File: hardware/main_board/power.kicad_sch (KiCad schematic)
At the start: 30 parts, among them J1 USB_C_Receptacle_USB2.0_16P, J2 Conn_01x03, J3 Conn_01x03, SW1 SW_Push, U1 USBLC6-2SC6, U2 BQ24259RGER, U3 TPS7A0533PDBV

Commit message: Fix PCB routing errors, update LED and connector footprints
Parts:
- D1, D2: footprint LED_SMD:LED_0603_1608Metric -> LED_SMD:LED_0805_2012Metric
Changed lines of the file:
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@@
 			)
 		)
-		(property "Footprint" "LED_SMD:LED_0603_1608Metric"
+		(property "Footprint" "LED_SMD:LED_0805_2012Metric"
 			(at 152.4 54.61 0)
 			(effects
@@
 			)
 		)
-		(property "Footprint" "LED_SMD:LED_0603_1608Metric"
+		(property "Footprint" "LED_SMD:LED_0805_2012Metric"
 			(at 142.24 54.61 0)
 			(effects

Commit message: Route 4-layer PCB
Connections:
- net D+: now also U1.1 (I/O1); no longer U1.3 (I/O2)
- net D-: now also U1.3 (I/O2); no longer U1.1 (I/O1)
- net USBCONN_D+: now also U1.6 (I/O1); no longer U1.4 (I/O2)
- net USBCONN_D-: now also U1.4 (I/O2); no longer U1.6 (I/O1)
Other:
- moved on the sheet: U1
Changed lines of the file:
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@@
 	(wire
 		(pts
-			(xy 59.69 127) (xy 59.69 125.73)
+			(xy 77.47 127) (xy 77.47 125.73)
 		)
 		(stroke
@@
 	(wire
 		(pts
-			(xy 59.69 125.73) (xy 62.23 125.73)
+			(xy 77.47 125.73) (xy 74.93 125.73)
 		)
 		(stroke
@@
 	(hierarchical_label "VBUS"
 		(shape input)
-		(at 74.93 125.73 0)
+		(at 62.23 125.73 180)
 		(effects
 			(font
 				(size 1.27 1.27)
 			)
-			(justify left)
+			(justify right)
 		)
 	)
@@
 	(symbol
 		(lib_id "power:GND")
-		(at 59.69 127 0)
+		(at 77.47 127 0)
+		(mirror y)
 		(unit 1)
 		(exclude_from_sim no)
@@
 		(fields_autoplaced yes)
 		(property "Reference" "#PWR3"
-			(at 59.69 133.35 0)
+			(at 77.47 133.35 0)
 			(effects
 				(font
@@
 		)
 		(property "Value" "GND"
-			(at 59.69 132.08 0)
+			(at 77.47 132.08 0)
 			(effects
 				(font
@@
 		)
 		(property "Footprint" ""
-			(at 59.69 127 0)
+			(at 77.47 127 0)
 			(effects
 				(font
@@
 		)
 		(property "Datasheet" ""
-			(at 59.69 127 0)
+			(at 77.47 127 0)
 			(effects
 				(font
@@
 		)
 		(property "Description" "Power symbol creates a global label with name \"GND\" , ground"
-			(at 59.69 127 0)
+			(at 77.47 127 0)
 			(effects
 				(font
@@
 	(symbol
 		(lib_id "Power_Protection:USBLC6-2SC6")
-		(at 69.85 125.73 270)
-		(mirror x)
+		(at 67.31 125.73 90)
 		(unit 1)
 		(exclude_from_sim no)
@@
 		(dnp no)
 		(property "Reference" "U1"
-			(at 79.756 122.428 90)
+			(at 58.674 129.794 90)
 			(effects
 				(font
@@
 		)
 		(property "Value" "USBLC6-2SC6"
-			(at 79.756 119.888 90)
+			(at 58.42 131.826 90)
 			(effects
 				(font
@@
 		)
 		(property "Footprint" "Package_TO_SOT_SMD:SOT-23-6"
-			(at 63.5 124.46 0)
+			(at 73.66 124.46 0)
 			(effects
 				(font
@@
 		)
 		(property "Datasheet" "https://www.st.com/resource/en/datasheet/usblc6-2.pdf"
-			(at 61.595 124.46 0)
+			(at 75.565 124.46 0)
 			(effects
 				(font
@@
 		)
 		(property "Description" "Very low capacitance ESD protection diode, 2 data-line, SOT-23-6"
-			(at 69.85 125.73 0)
+			(at 67.31 125.73 0)
 			(effects
 				(font
@@
 		)
 		(property "JLCPCB" "C7519"
-			(at 69.85 125.73 0)
-			(effects
-				(font
+			(at 67.31 125.73 0)
+			(effects
+				(font

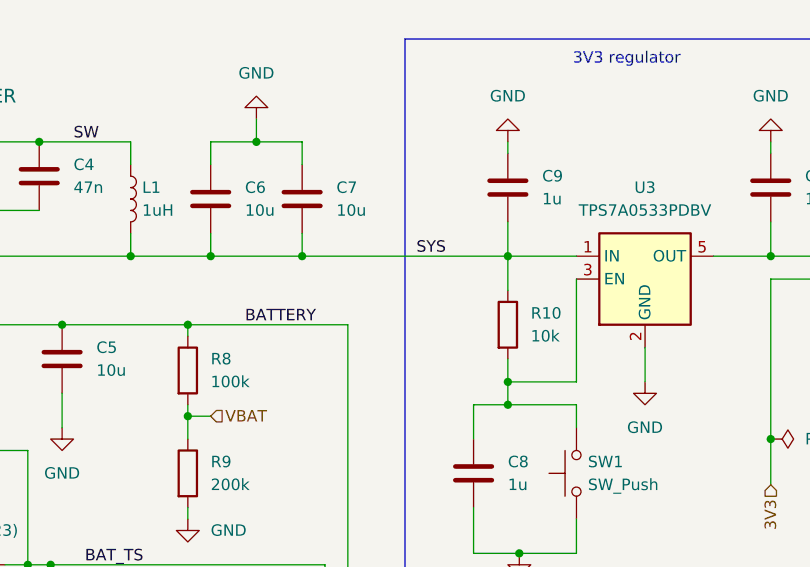
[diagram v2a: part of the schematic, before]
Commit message: Add SYS power to the extension socket
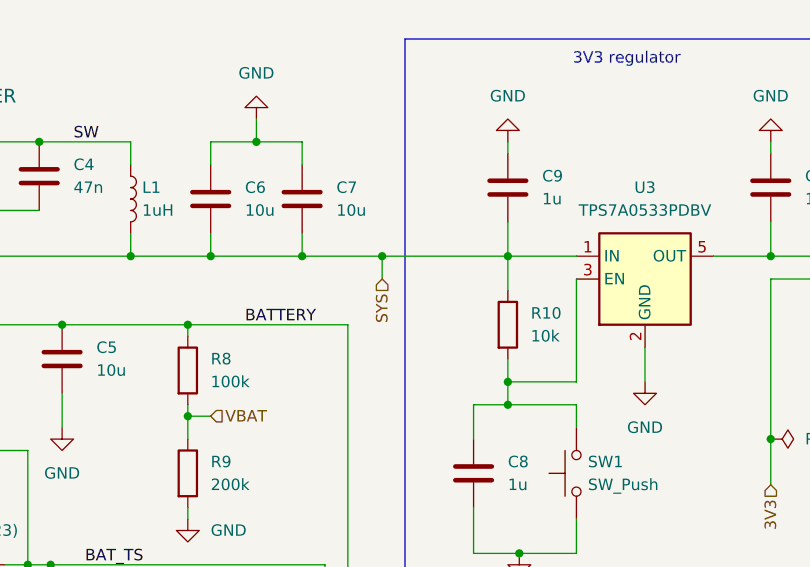
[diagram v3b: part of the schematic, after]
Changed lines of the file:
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@@
+	)
+	(junction
+		(at 207.01 95.25)
+		(diameter 0)
+		(color 0 0 0 0)
 	)
 	(junction
@@
 	(wire
 		(pts
-			(xy 198.12 95.25) (xy 220.98 95.25)
+			(xy 198.12 95.25) (xy 207.01 95.25)
 		)
 		(stroke
@@
 	(wire
 		(pts
+			(xy 207.01 95.25) (xy 207.01 97.79)
+		)
+		(stroke
+			(width 0)
+			(type default)
+		)
+	)
+	(wire
+		(pts
 			(xy 185.42 111.76) (xy 185.42 113.03)
 		)
@@
 		(pts
 			(xy 96.52 87.63) (xy 121.92 87.63)
+		)
+		(stroke
+			(width 0)
+			(type default)
+		)
+	)
+	(wire
+		(pts
+			(xy 207.01 95.25) (xy 220.98 95.25)
 		)
 		(stroke
@@
 	(label "USBCONN_D+"
 		(at 67.31 114.3 90)
-		(effects
-			(font
-				(size 1.27 1.27)
-			)
-			(justify left bottom)
-		)
-	)
-	(label "SYS"
-		(at 210.82 95.25 0)
 		(effects
 			(font
@@
 		(effects
 			(font
+				(size 1.27 1.27)
+			)
+			(justify right)
+		)
+	)
+	(hierarchical_label "SYS"
+		(shape input)
+		(at 207.01 97.79 270)
+		(effects
+			(font
